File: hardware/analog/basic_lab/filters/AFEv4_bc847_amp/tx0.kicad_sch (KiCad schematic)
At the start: 2 parts, among them J2 Connector_Generic_Conn_01x02, J9 Connector_Generic_Conn_01x02

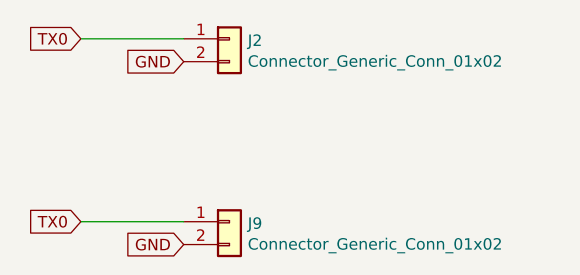
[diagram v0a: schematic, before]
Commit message: started PCB LC LPF
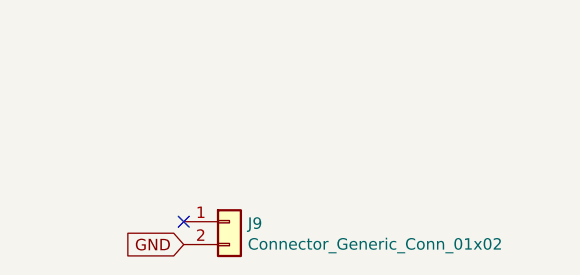
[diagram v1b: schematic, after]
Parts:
- removed J2: Connector_Generic_Conn_01x02, Connector_PinHeader_2.54mm:PinHeader_1x02_P2.54mm_Vertical, symbol bgt:Connector_Generic_Conn_01x02
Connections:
- net TX0: no longer names the net of J9.1 (Pin_1)
- no-connect marks 0 -> 1
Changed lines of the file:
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@@
 (kicad_sch (version 20211123) (generator eeschema)
   (paper "A4")
-  (wire (pts (xy 83.82 69.85) (xy 95.25 69.85))
-    (stroke (width 0) (type default) (color 0 0 0 0))
-  )
-  (wire (pts (xy 83.82 90.17) (xy 95.25 90.17))
-    (stroke (width 0) (type default) (color 0 0 0 0))
-  )
-  (global_label "TX0" (shape input) (at 83.82 90.17 180) (fields_autoplaced)
-    (effects (font (size 1.27 1.27)) (justify right))
-    (property "Intersheet References" "${INTERSHEET_REFS}" (id 0) (at 78.1091 90.0906 0)
-      (effects (font (size 1.27 1.27)) (justify right) hide)
-    )
-  )
+  (no_connect (at 95.25 90.17))
   (global_label "GND" (shape input) (at 95.25 92.71 180) (fields_autoplaced)
     (effects (font (size 1.27 1.27)) (justify right))
@@
     )
   )
-  (global_label "GND" (shape input) (at 95.25 72.39 180) (fields_autoplaced)
-    (effects (font (size 1.27 1.27)) (justify right))
-    (property "Intersheet References" "${INTERSHEET_REFS}" (id 0) (at -35.56 13.97 0)
-      (effects (font (size 1.27 1.27)) hide)
-    )
-  )
-  (global_label "TX0" (shape input) (at 83.82 69.85 180) (fields_autoplaced)
-    (effects (font (size 1.27 1.27)) (justify right))
-    (property "Intersheet References" "${INTERSHEET_REFS}" (id 0) (at 78.1091 69.7706 0)
-      (effects (font (size 1.27 1.27)) (justify right) hide)
-    )
-  )
-  (symbol (lib_id "bgt:Connector_Generic_Conn_01x02") (at 100.33 69.85 0) (unit 1)
-    (in_bom yes) (on_board yes)
-    (property "Reference" "J2" (id 0) (at 102.362 70.0532 0)
-      (effects (font (size 1.27 1.27)) (justify left))
-    )
-    (property "Value" "Connector_Generic_Conn_01x02" (id 1) (at 102.362 72.3646 0)
-      (effects (font (size 1.27 1.27)) (justify left))
-    )
-    (property "Footprint" "Connector_PinHeader_2.54mm:PinHeader_1x02_P2.54mm_Vertical" (id 2) (at 100.33 69.85 0)
-      (effects (font (size 1.27 1.27)) hide)
-    )
-    (property "Datasheet" "" (id 3) (at 100.33 69.85 0)
-      (effects (font (size 1.27 1.27)) hide)
-    )
-    (pin "1")
-    (pin "2")
-  )
   (symbol (lib_id "bgt:Connector_Generic_Conn_01x02") (at 100.33 90.17 0) (unit 1)
